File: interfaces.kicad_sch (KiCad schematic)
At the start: 61 parts, among them J2 JST-SH 1x08, J3 Digital_VTX_Connector, J4 UJ20-C-H-G-SMT-5-P16-TR, P1 4V5, P10 R1, P11 +, P12 C, P13 R5, P14 M1, P15 M2, P16 M3, P17 M4, P18 G, P19 5V, P2 G, P20 G, P21 VI, P22 5V, P23 G, P24 T5, P25 R5, P26 5V, P27 LED, P28 G, P29 5V, P3 SCL, P30 -B, P31 G, P32 T2, P33 R2, P34 R1, P35 G, P36 G, P37 9V, P38 5V, P39 G, P4 SDA, P40 5V, P41 G, P42 T5, P43 T5, P5 T3, P6 R3, P7 4V5, P8 G, P9 T1, Q1 NX138AKMYL

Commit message: Add return vias for SPI and fixed some rouding traces
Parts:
- removed H1, H2, H3, H4: MountingHole, 0_mechanical:MountingHole_M4_Gummy6mm, symbol Mechanical:MountingHole

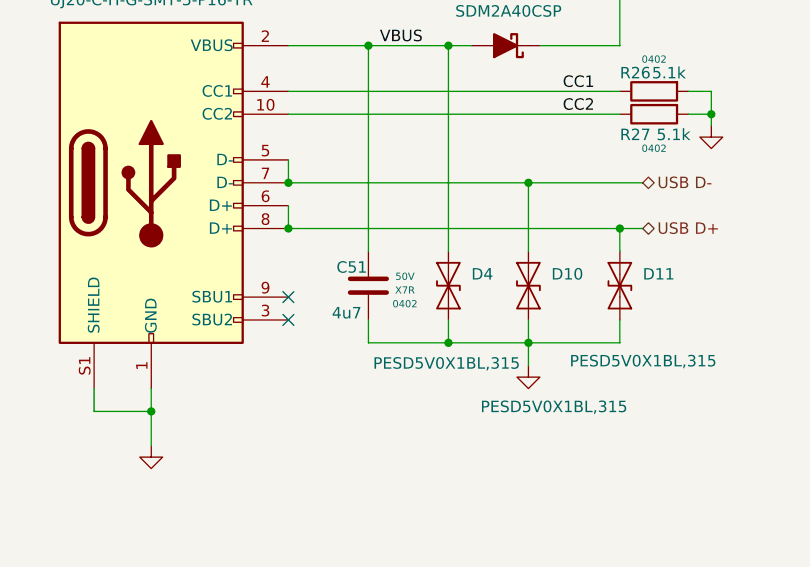
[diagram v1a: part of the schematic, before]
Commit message: Crystal change, gnd cut-out for crystal, bom update
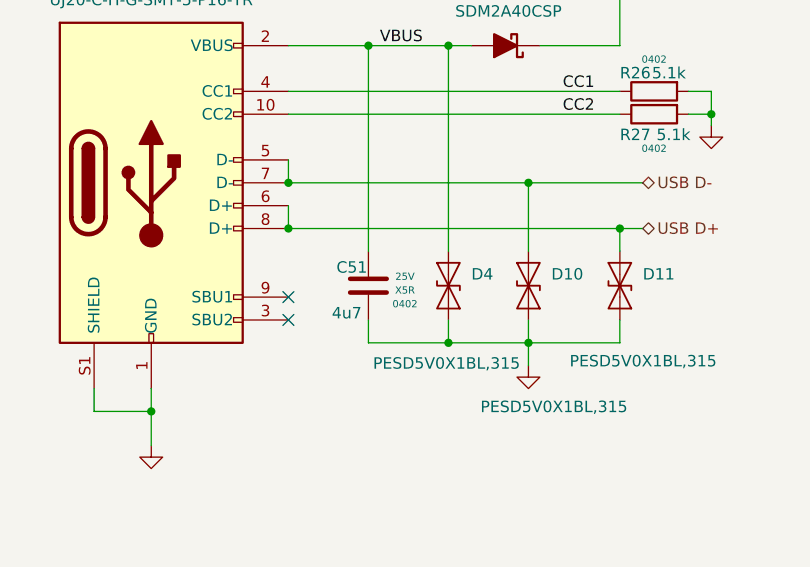
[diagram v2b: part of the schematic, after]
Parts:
- C51: JLCPCB # C437568 -> C385032; MANUFACTURER # GRM31CR71H475KA12L -> GRM155R61E225KE11D; Temp Coef X7R -> X5R; Unit Price 0.3533 -> (none); Voltage 50V -> 25V
- D2: Unit Price 0.1839 -> (none)
- J2: Unit Price 0.1161 -> (none)
- J3: Unit Price 0.3062 -> (none)
- J4: Unit Price 0.63 -> (none)
- R25: JLCPCB # C138040 -> C60490; MANUFACTURER # RC0402FR-071K2L -> RC0402FR-0710KL; Unit Price 0.0006 -> (none)
- R26, R27: Unit Price 0.0008 -> (none)

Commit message: Updated
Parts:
- C51: JLCPCB # C385032 -> (none); LCSC (none) -> C426094; MANUFACTURER # GRM155R61E225KE11D -> GRM155R61C475KE15D
- D10, D11, D4: value PESD5V0X1BL,315 -> PESD5V0F1BRLDYL; LCSC (none) -> C552549; MANUFACTURER (none) -> Nexperia; MANUFACTURER # (none) -> PESD5V0F1BRLDYL
- D2: JLCPCB # C1973133 -> (none); LCSC (none) -> C1973133
- D3: LCSC (none) -> C6671609; MANUFACTURER (none) -> Diodes; MANUFACTURER # (none) -> SDM2A40CSP-7B
- J2: JLCPCB # C2845367 -> (none); LCSC (none) -> C2845367
- J3: JLCPCB # C160405 -> (none); LCSC (none) -> C160405
- J4: JLCPCB # C530612 -> (none); LCSC (none) -> C530612
- JP2: now left out of the parts list
- Q1: LCSC (none) -> C3290147; MANUFACTURER (none) -> Nexperia; MANUFACTURER # (none) -> NX138AKMYL
- R25: JLCPCB # C60490 -> (none); LCSC (none) -> C60490
- R26, R27: JLCPCB # C227396 -> (none); LCSC (none) -> C227396
